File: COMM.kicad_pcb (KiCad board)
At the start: 4 copper layers, 90.2 x 95.9 mm, 41 parts, among them IC1 TLV61047DDCR, IC2 Voltage Converter (ADP7158ARD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, J1 SMA Conn. (RFPC-SMA30-F), U1 XBee Module (XBP9B-DMSTB002), U2 DMR Module (DMR818S-5W)

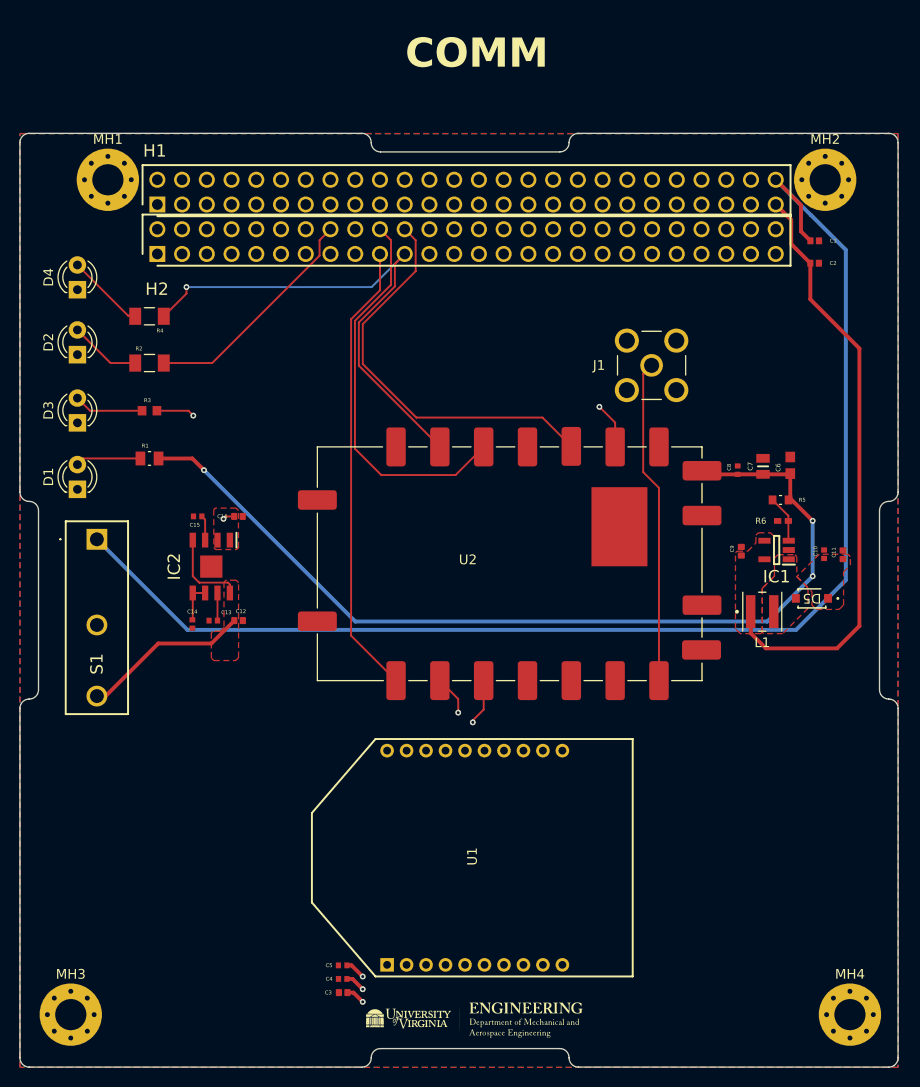
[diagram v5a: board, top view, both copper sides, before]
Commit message: Swapped H1 and H2 spacebuses and rewired according to the swap.
Signed-off-by: Logan Tolbert <xem6df@virginia.edu>
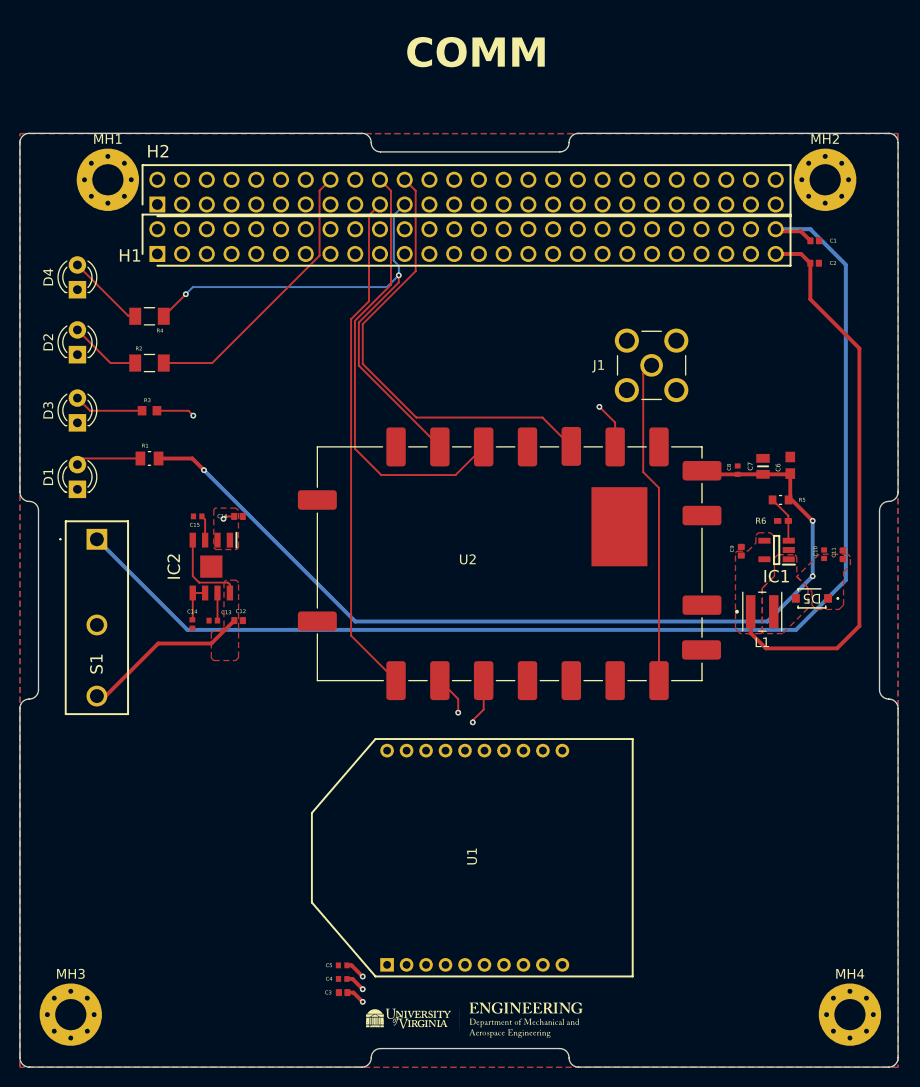
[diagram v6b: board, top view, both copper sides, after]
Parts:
- moved H1 5.08 mm to (115.7, 65.7)
- moved H2 5.08 mm to (115.7, 60.6)
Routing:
- net /Associate/DIO5_XB: track 88.8 -> 98.9 mm
- net +5V: track 134.7 -> 128.0 mm
- net /DIN/CONFIG/DIO14_XB: track 89.6 -> 95.6 mm
- net /UART_TX_DMR: track 54.6 -> 59.7 mm
- net /ON_SLEEP/DIO9_XB: track 70.0 -> 75.1 mm
- net /DTR/SLEEP_RQ/DIO8_XB: track 85.2 -> 90.3 mm
- net /DOUT/DIO13_XB: track 86.1 -> 91.2 mm
- net /MIC_IN_DMR: track 47.0 -> 52.0 mm
- net /UART_RX_DMR: track 57.9 -> 63.0 mm
- net /RESET_XB: track 84.7 -> 89.8 mm
- net /PTT_DMR: track 41.5 -> 46.6 mm
- net /LINE_OUT_DMR: track 40.1 -> 45.2 mm
- net /T/R_DMR: track 53.0 -> 56.6 mm, vias 1 -> 2
- net /TLV61047/VIN: track 61.8 -> 58.2 mm

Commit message: Updated COMM board to account for errors found during testing
Signed-off-by: Logan Tolbert <xem6df@virginia.edu>
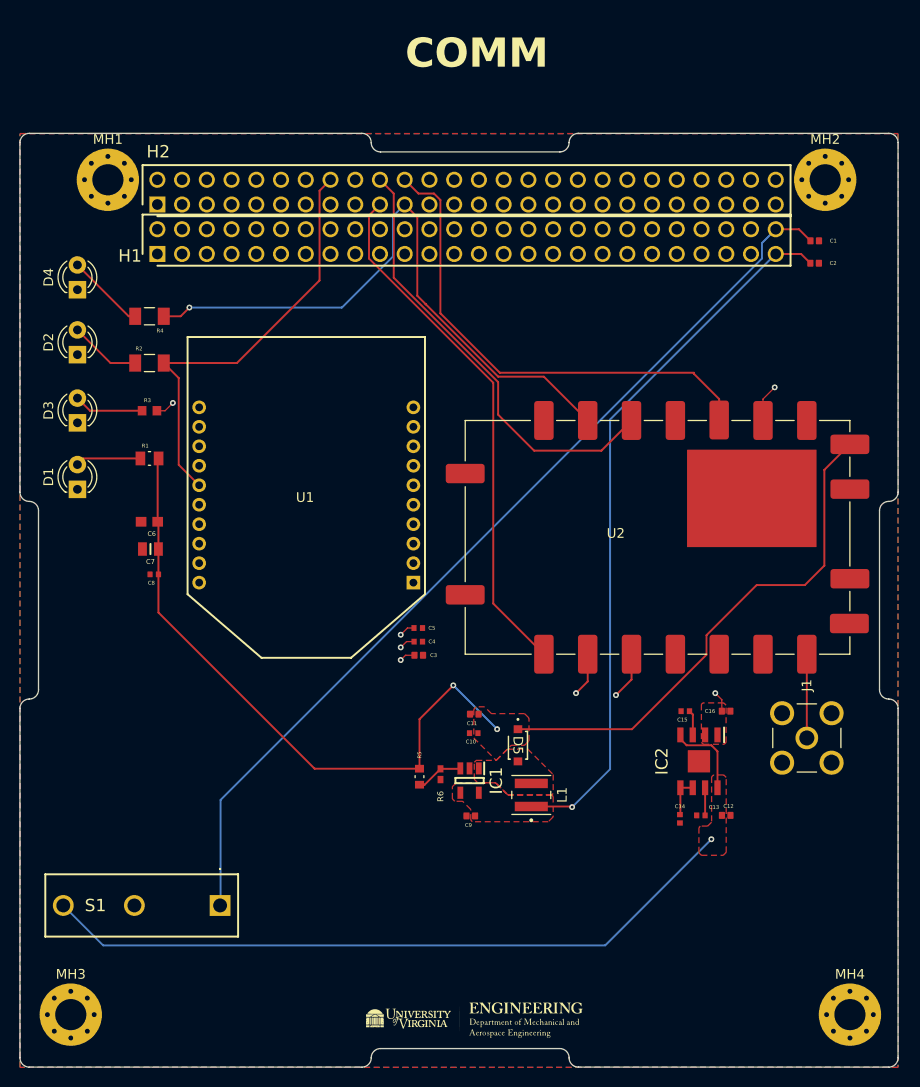
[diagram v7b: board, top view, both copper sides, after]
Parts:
- moved C6 66.1 mm to (114.9, 93.2), turned to 180 degrees
- moved C7 63.5 mm to (115.0, 96.0), turned to 180 degrees
- moved C8 60.9 mm to (115.4, 98.6), turned to 180 degrees
- moved C12 53.9 mm to (174.1, 123.3)
- moved C14 53.9 mm to (169.4, 123.7)
- moved C16 53.9 mm to (174.1, 112.7)
- moved C15 53.9 mm to (169.9, 112.7)
- moved IC2 53.9 mm to (171.3, 117.8)
- moved C13 53.9 mm to (171.5, 123.3)
- moved R5 46.7 mm to (142.6, 119.4), turned to -90 degrees
- moved R6 43.7 mm to (144.8, 119.1), turned to -90 degrees
- moved J1 41.4 mm to (182.4, 115.4), turned to 0 degrees
- moved C11 41.3 mm to (148.3, 113.0), turned to 180 degrees
- moved U1 40.7 mm to (131.0, 90.7), turned to 180 degrees
- moved C10 40.4 mm to (148.2, 114.9), turned to 180 degrees
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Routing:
- net /DTR/SLEEP_RQ/DIO8_XB: track 90.3 -> 29.5 mm
- net /Voltage Converter/VIN: track 26.1 -> 81.3 mm, vias 0 -> 1
- net /Associate/DIO5_XB: track 98.9 -> 44.4 mm
- net /RESET_XB: track 89.8 -> 35.4 mm
- net /DIN/CONFIG/DIO14_XB: track 95.6 -> 45.7 mm
- net /ON_SLEEP/DIO9_XB: track 75.1 -> 28.3 mm
- net /DOUT/DIO13_XB: track 91.2 -> 51.2 mm
- net +5V: track 128.0 -> 97.1 mm
- net /DMR818S 5W RF Module/ANT: track 33.4 -> 8.60 mm
- net +8V: track 97.8 -> 118.8 mm, vias 3 -> 2
- net /TLV61047/VIN: track 58.2 -> 73.6 mm, vias 0 -> 1
- net /T/R_DMR: track 56.6 -> 64.7 mm, vias 2 -> 1
- net /UART_RX_DMR: track 63.0 -> 67.8 mm
- net /PTT_DMR: track 46.6 -> 50.6 mm
- net +3.3V: track 16.1 -> 12.9 mm
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
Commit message: Updated LEDs and associated resistors on board. COMM board is ready to be reordered.
Signed-off-by: Logan Tolbert <xem6df@virginia.edu>
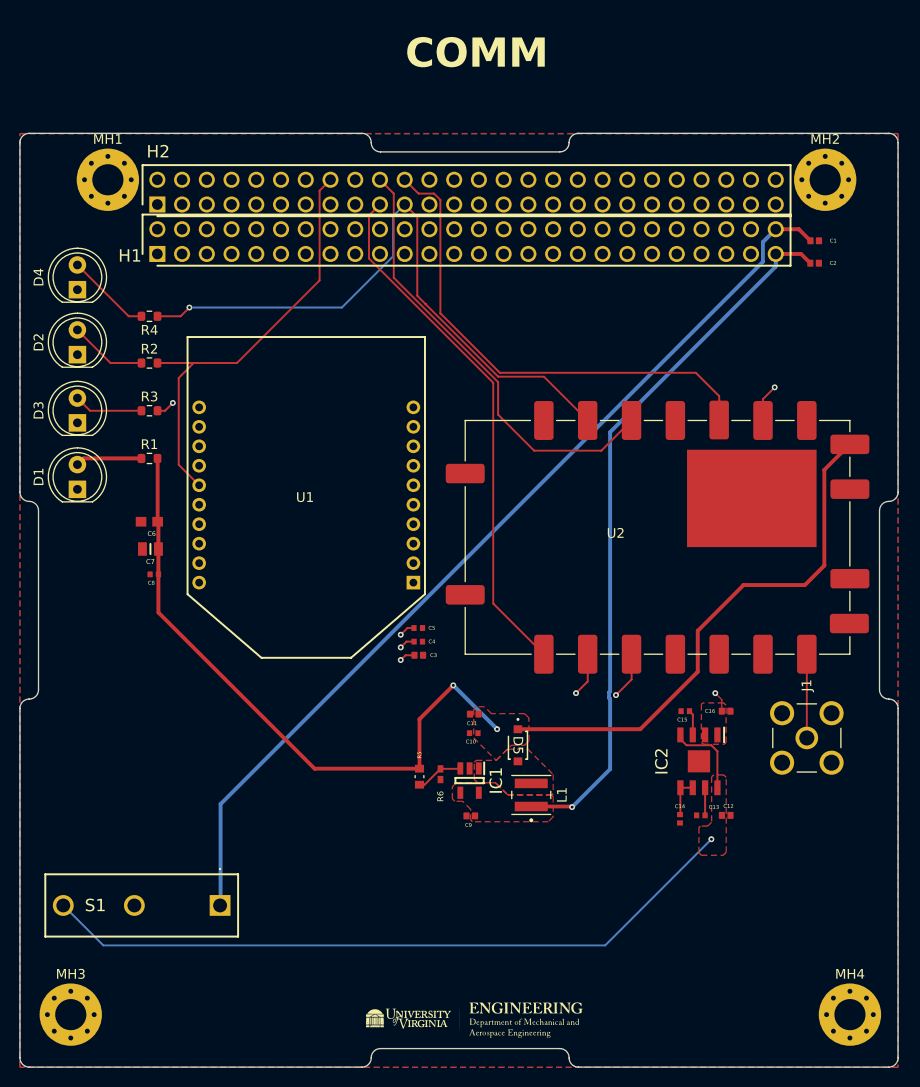
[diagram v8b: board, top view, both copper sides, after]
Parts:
- D1, D2, D3, D4: footprint LED_THT:LED_D3.0mm -> LED_THT:LED_D5.0mm
- R1: value 250 Ω -> 220 Ω; footprint R_250O:RESC2012X65N -> Resistor_SMD:R_0603_1608Metric
- R2, R4: value 140 Ω -> 62 Ω; footprint R_140O:RESC3216X70N -> Resistor_SMD:R_0603_1608Metric
- R3: value 110 Ω -> 62 Ω; footprint R_110O:RESC1508X55N -> Resistor_SMD:R_0603_1608Metric
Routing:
- net /Associate/DIO5_XB: track 44.4 -> 49.1 mm
- net +8V: track 118.8 -> 120.1 mm
- net /DIN/CONFIG/DIO14_XB: track 45.7 -> 46.6 mm
- net Net-(D4-A): track 8.12 -> 8.76 mm
- net Net-(D2-A): track 7.34 -> 7.98 mm
- net /T/R_DMR: track 64.7 -> 65.3 mm
